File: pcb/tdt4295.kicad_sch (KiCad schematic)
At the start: 1 part, among them U2 TPS54325PWP

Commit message: pcb: add mcu component and sheet
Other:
- added sheet MCU (MCU.kicad_sch)
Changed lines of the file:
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@@
+	)
+	(sheet
+		(at 25.4 62.23)
+		(size 25.4 16.51)
+		(exclude_from_sim no)
+		(in_bom yes)
+		(on_board yes)
+		(dnp no)
+		(fields_autoplaced yes)
+		(stroke
+			(width 0.1524)
+			(type solid)
+		)
+		(fill
+			(color 0 0 0 0)
+		)
+		(property "Sheetname" "MCU"
+			(at 25.4 61.5184 0)
+			(show_name no)
+			(do_not_autoplace no)
+			(effects
+				(font
+					(size 1.27 1.27)
+				)
+				(justify left bottom)
+			)
+		)
+		(property "Sheetfile" "MCU.kicad_sch"
+			(at 25.4 79.3246 0)
+			(show_name no)
+			(do_not_autoplace no)
+			(effects
+				(font
+					(size 1.27 1.27)
+				)
+				(justify left top)
+			)
+		)
+		(instances
+			(project "tdt4295"
+				(path "/603dd496-f9c4-4a31-9104-19eec41ebc98"
+					(page "5")
+				)
+			)
+		)
 	)
 	(sheet

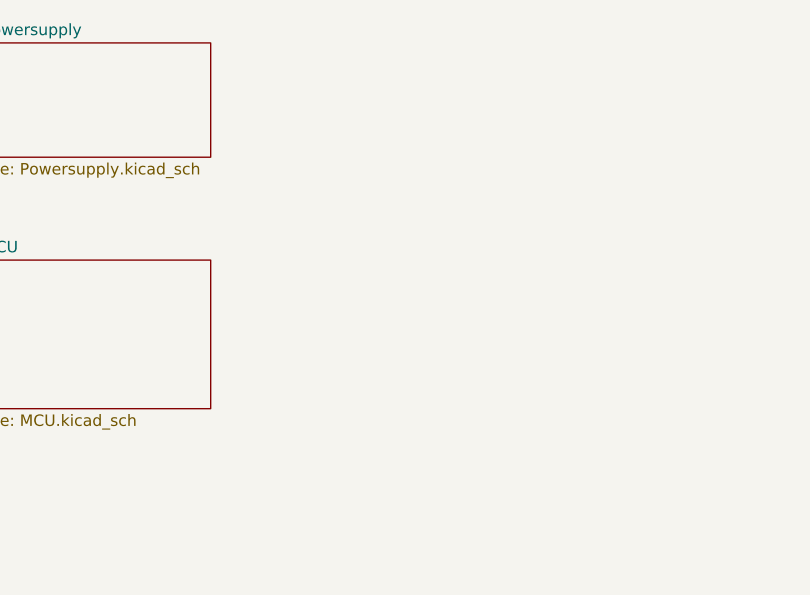
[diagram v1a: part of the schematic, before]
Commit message: pcb: changes usbc and add input power
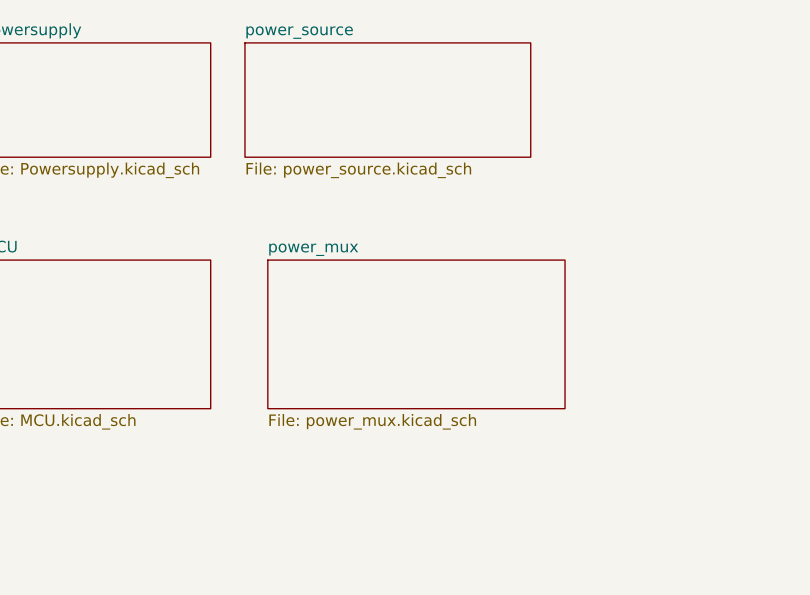
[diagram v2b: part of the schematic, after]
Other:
- added sheet power_mux (power_mux.kicad_sch)
- added sheet power_source (power_source.kicad_sch)
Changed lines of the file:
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@@
+	)
+	(sheet
+		(at 54.61 38.1)
+		(size 31.75 12.7)
+		(exclude_from_sim no)
+		(in_bom yes)
+		(on_board yes)
+		(dnp no)
+		(fields_autoplaced yes)
+		(stroke
+			(width 0.1524)
+			(type solid)
+		)
+		(fill
+			(color 0 0 0 0)
+		)
+		(property "Sheetname" "power_source"
+			(at 54.61 37.3884 0)
+			(show_name no)
+			(do_not_autoplace no)
+			(effects
+				(font
+					(size 1.27 1.27)
+				)
+				(justify left bottom)
+			)
+		)
+		(property "Sheetfile" "power_source.kicad_sch"
+			(at 54.61 51.3846 0)
+			(show_name no)
+			(do_not_autoplace no)
+			(effects
+				(font
+					(size 1.27 1.27)
+				)
+				(justify left top)
+			)
+		)
+		(instances
+			(project "tdt4295"
+				(path "/603dd496-f9c4-4a31-9104-19eec41ebc98"
+					(page "7")
+				)
+			)
+		)
 	)
 	(sheet
@@
 				)
 			)
+		)
+	)
+	(sheet
+		(at 57.15 62.23)
+		(size 33.02 16.51)
+		(exclude_from_sim no)
+		(in_bom yes)
+		(on_board yes)
+		(dnp no)
+		(fields_autoplaced yes)
+		(stroke
+			(width 0.1524)
+			(type solid)
+		)
+		(fill
+			(color 0 0 0 0)
+		)
+		(property "Sheetname" "power_mux"
+			(at 57.15 61.5184 0)
+			(show_name no)
+			(do_not_autoplace no)
+			(effects
+				(font
+					(size 1.27 1.27)
+				)
+				(justify left bottom)
+			)
+		)
+		(property "Sheetfile" "power_mux.kicad_sch"
+			(at 57.15 79.3246 0)
+			(show_name no)
+			(do_not_autoplace no)
+			(effects
+				(font
+					(size 1.27 1.27)
+				)
+				(justify left top)
+			)
+		)
+		(instances
+			(project "tdt4295"
+				(path "/603dd496-f9c4-4a31-9104-19eec41ebc98"
+					(page "9")
+				)
+			)

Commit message: pcb: create fpga
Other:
- added sheet FPGA (fpga.kicad_sch)
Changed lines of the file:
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@@
+		)
+	)
+	(sheet
+		(at 85.09 114.3)
+		(size 35.56 22.225)
+		(exclude_from_sim no)
+		(in_bom yes)
+		(on_board yes)
+		(dnp no)
+		(fields_autoplaced yes)
+		(stroke
+			(width 0.1524)
+			(type solid)
+		)
+		(fill
+			(color 0 0 0 0)
+		)
+		(property "Sheetname" "FPGA"
+			(at 85.09 113.5884 0)
+			(show_name no)
+			(do_not_autoplace no)
+			(effects
+				(font
+					(size 1.27 1.27)
+				)
+				(justify left bottom)
+			)
+		)
+		(property "Sheetfile" "fpga.kicad_sch"
+			(at 85.09 137.1096 0)
+			(show_name no)
+			(do_not_autoplace no)
+			(effects
+				(font
+					(size 1.27 1.27)
+				)
+				(justify left top)
+			)
+		)
+		(instances
+			(project "tdt4295"
+				(path "/603dd496-f9c4-4a31-9104-19eec41ebc98"
+					(page "10")
+				)
+			)
 		)
 	)

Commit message: pcb: add sram sheet
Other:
- added sheet SRAM (sram.kicad_sch)
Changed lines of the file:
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@@
+	)
+	(sheet
+		(at 114.3 95.25)
+		(size 33.655 13.335)
+		(exclude_from_sim no)
+		(in_bom yes)
+		(on_board yes)
+		(dnp no)
+		(fields_autoplaced yes)
+		(stroke
+			(width 0.1524)
+			(type solid)
+		)
+		(fill
+			(color 0 0 0 0)
+		)
+		(property "Sheetname" "SRAM"
+			(at 114.3 94.5384 0)
+			(show_name no)
+			(do_not_autoplace no)
+			(effects
+				(font
+					(size 1.27 1.27)
+				)
+				(justify left bottom)
+			)
+		)
+		(property "Sheetfile" "sram.kicad_sch"
+			(at 114.3 109.1696 0)
+			(show_name no)
+			(do_not_autoplace no)
+			(effects
+				(font
+					(size 1.27 1.27)
+				)
+				(justify left top)
+			)
+		)
+		(instances
+			(project "tdt4295"
+				(path "/603dd496-f9c4-4a31-9104-19eec41ebc98"
+					(page "11")
+				)
+			)
+		)
 	)
 	(sheet
